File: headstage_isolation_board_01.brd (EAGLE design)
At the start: 100 x 80 mm, 15 parts

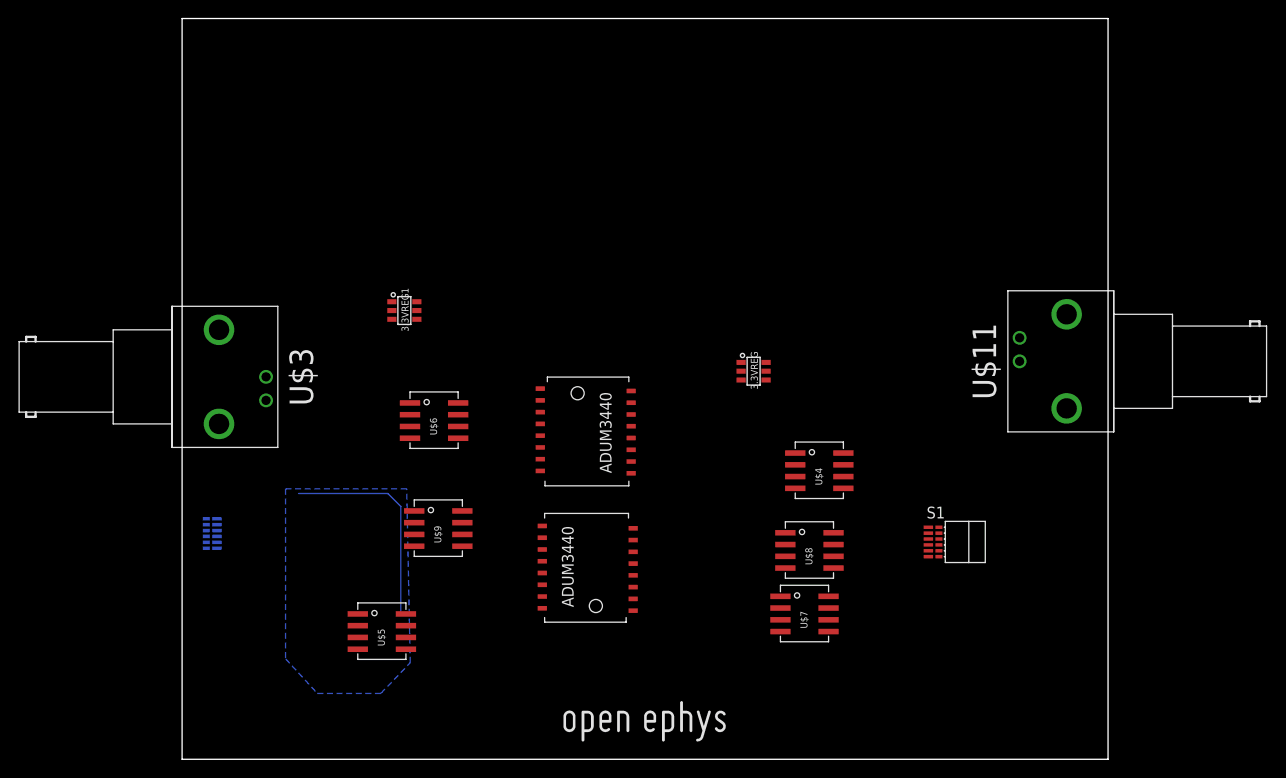
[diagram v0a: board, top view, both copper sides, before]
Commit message: added DC-DC converter
still missing resistors etc
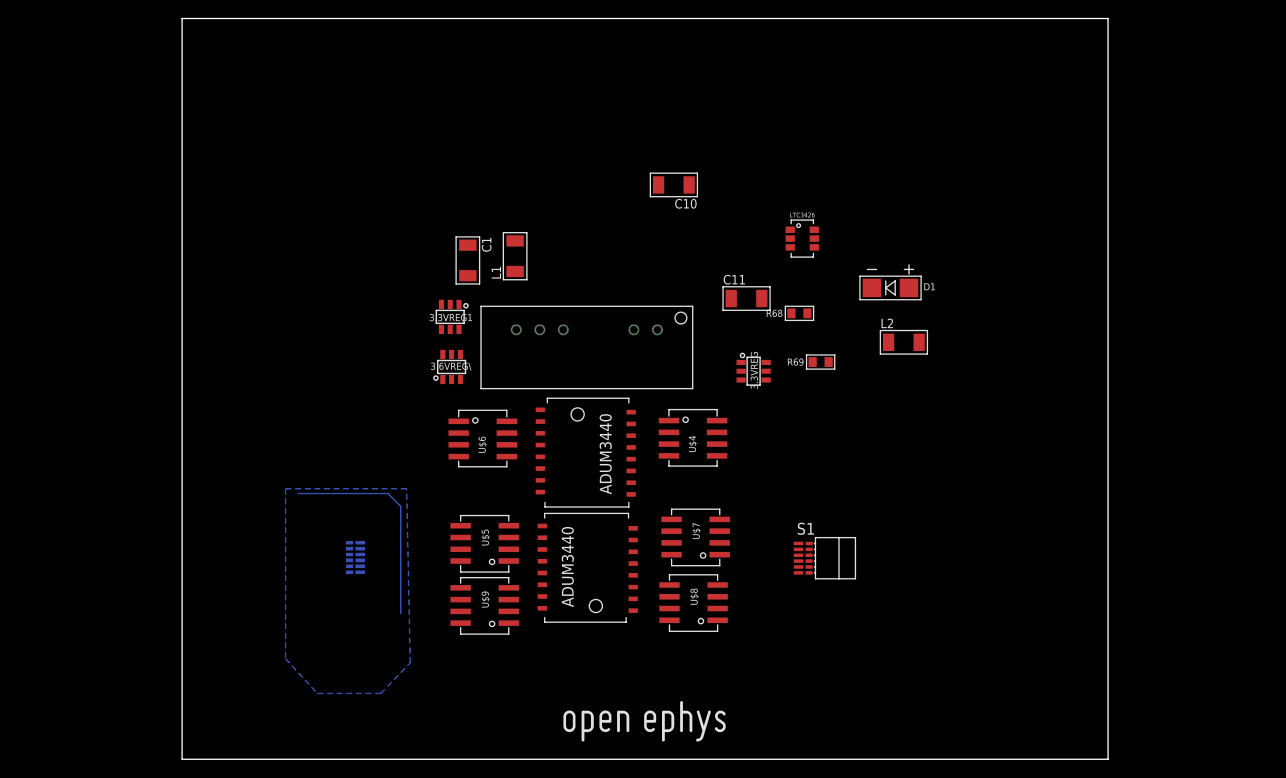
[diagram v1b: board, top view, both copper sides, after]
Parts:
- removed U$11, U$3: BNC_RIGHT_ANGLE, open-ephys_old:BNC_RIGHT_ANGLE
- added 3.6VREG\: TPS79301, RHD2000_eval_board:SOT-23-6
- added 5.5V_BOOST: LTC3426, open-ephys:SOT23-6
- added C1: 1u, RHD2000_eval_board:1206
- added C10, C11: 10u, RHD2000_eval_board:1206
- added D1: MBRA210LT3-D, open-ephys:MBRA210LT3-D
- added L1: 22uH, RHD2000_eval_board:1206
- added L2: (no value), RHD2000_eval_board:1206
- added R68: 95.3k, RHD2000_eval_board:0603
- added R69: 27.4k, RHD2000_eval_board:0603
- added U$12: NMV0505, open-ephys:NMV0505
- moved U$5 21.1 mm to (35.3, 25.2), turned to 180 degrees
- moved S2 15.7 mm to (17.1, 21.8)
- moved S1 14.1 mm to (68.7, 21.7)
- moved U$4 14.1 mm to (52.6, 32.8)
- moved U$7 13.8 mm to (58.1, 25.9), turned to 180 degrees
- moved U$9 11.2 mm to (35.3, 18.5), turned to 180 degrees
- moved U$8 7.54 mm to (57.8, 18.8), turned to 180 degrees
- moved U$6 5.62 mm to (29.9, 32.7)
- moved 3.3VREG1 5.00 mm to (29.0, 47.8), turned to 270 degrees
- moved U$10 2.29 mm to (42.7, 33.7)
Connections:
- removed net IN: 3.3VREG1.1
- removed net N$31: 3.3VREG.1, S1.T6
- new net 5VBOOST: 3.3VREG.1, 5.5V_BOOST.5, C11.1, D1.NEG, R68.2, U$12.P$1
- new net N$276: 5.5V_BOOST.3, R68.1, R69.2
- new net N$278: 5.5V_BOOST.1, D1.POS, L2.2
- new net N$32: L1.1, U$12.P$7
- new net N$34: 3.3VREG1.1, 3.6VREG\.1, C1.1, L1.2
- new net VDD_IN: 5.5V_BOOST.4, 5.5V_BOOST.6, C10.1, L2.1, S1.T6
- net GND: now also 5.5V_BOOST.2, C10.2, C11.2, R69.1, U$12.P$2; no longer U$11.P$GND
- net GND_ISOLATED: now also 3.6VREG\.2, C1.2, U$10.P2, U$10.P8, U$12.P$5, U$2.P15, U$2.P9, U$5.P4, U$6.P5, U$9.P4; no longer U$3.P$GND
- net VDD33_ISOLATED: now also U$10.P1, U$2.P16, U$5.P1, U$6.P8, U$9.P1
- net VDD_ISOLATED: now also 3.6VREG\.6

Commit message: initial partial layout, added some regulator parts
still need to change r values for regulators
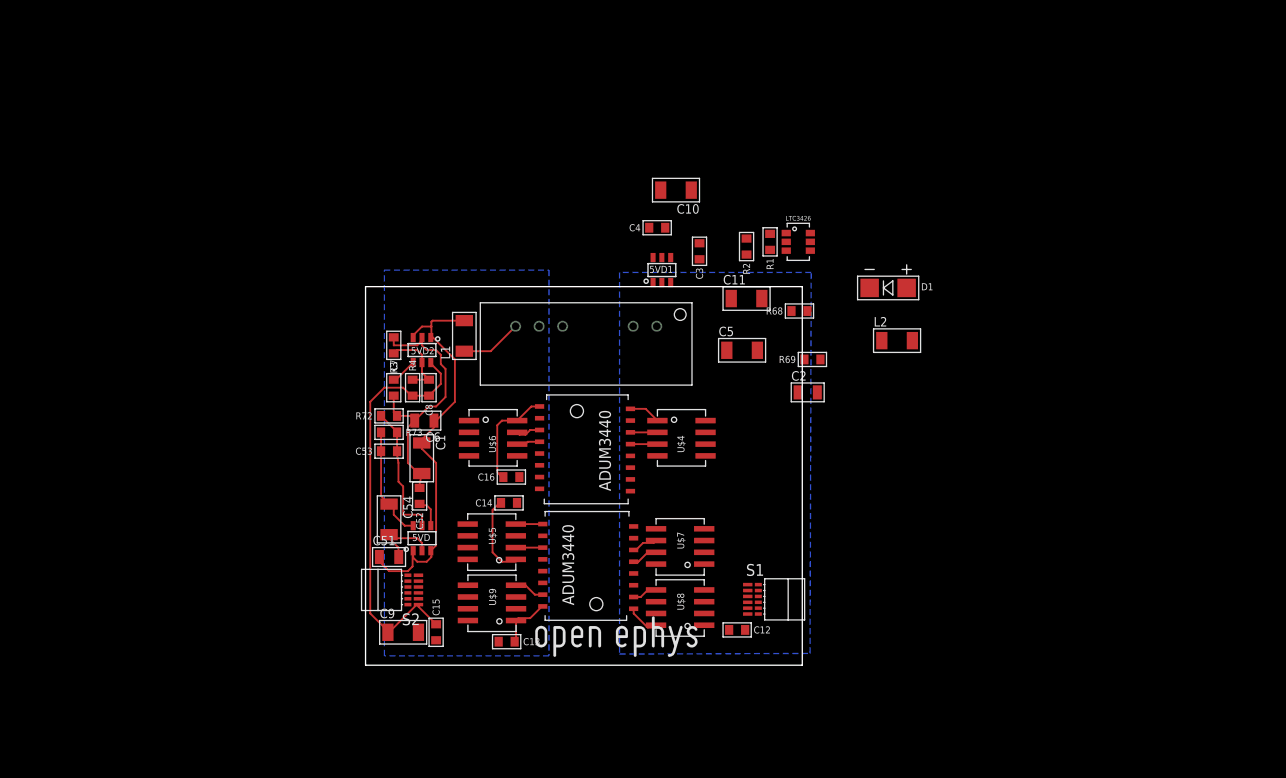
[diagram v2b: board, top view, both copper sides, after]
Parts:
- removed 3.3VREG, 3.3VREG1, 3.6VREG\: TPS79301, RHD2000_eval_board:SOT-23-6
- added 5VD, 5VD1, 5VD2: TPS79301, RHD2000_eval_board:SOT-23-6
- added C12, C13, C14, C15, C16: 100n, RHD2000_eval_board:0603
- added C2, C51, C6: 1.0u, RHD2000_eval_board:0805
- added C3, C52, C7: 10n, RHD2000_eval_board:0603
- added C4, C53, C8: 15p, RHD2000_eval_board:0603
- added C5, C54, C9: 22u, RHD2000_eval_board:1206
- added R1, R3, R72: 30.9k, RHD2000_eval_board:0603
- added R2, R4, R73: 95.3k, RHD2000_eval_board:0603
- moved C1 21.9 mm to (25.9, 32.5)
- moved L1 10.2 mm to (30.5, 45.7)
- moved U$1 9.64 mm to (37.5, 10.6)
- moved S2 7.21 mm to (23.4, 18.3), flipped to the top, turned to 90 degrees
- moved S1 7.06 mm to (63.2, 17.3)
- moved U$7 1.96 mm to (56.4, 24.9)
- moved U$8 1.54 mm to (56.4, 18.3)
- moved U$4 1.24 mm to (51.3, 32.8)
- moved U$6 1.12 mm to (31.0, 32.8)
- moved R69 0.93 mm to (68.1, 43.2)
- moved U$9 0.84 mm to (36.1, 18.8)
- moved U$5 0.78 mm to (36.0, 25.4)
- moved L2 0.76 mm to (77.2, 45.2)
- moved C10 0.60 mm to (53.3, 61.5)
- moved 5.5V_BOOST 0.56 mm to (66.5, 55.9)
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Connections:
- removed net N$34: 3.3VREG1.1, 3.6VREG\.1, C1.1, L1.2
- new net 5V_ISOLATED: 5VD.1, 5VD.3, 5VD2.1, 5VD2.3, C1.1, C51.1, C6.1, L1.2
- new net GND4: C15.2
- new net N$108: 5VD.5, C53.2, R72.1, R73.1
- new net N$33: 5VD1.4, C3.1
- new net N$35: 5VD1.5, C4.2, R1.1, R2.1
- new net N$36: 5VD2.4, C7.1
- new net N$37: 5VD2.5, C8.2, R3.1, R4.1
- new net N$97: 5VD.4, C52.1
- net 5VBOOST: now also 5VD1.1, 5VD1.3, C2.1; no longer 3.3VREG.1
- net GND: now also 5VD1.2, C12.1, C2.2, C3.2, C5.2, R1.2; no longer 3.3VREG.2
- net GND_ISOLATED: now also 5VD.2, 5VD2.2, C13.2, C14.2, C16.2, C51.2, C52.2, C54.2, C6.2, C7.2, C9.2, R3.2, R72.2, U$12.P$6; no longer 3.3VREG1.2, 3.6VREG\.2
- net VDD33: now also 5VD1.6, C12.2, C4.1, C5.1, R2.2; no longer 3.3VREG.6
- net VDD33_ISOLATED: now also 5VD.6, C13.1, C14.1, C16.1, C53.1, C54.1, R73.2; no longer 3.3VREG1.6
- net VDD_ISOLATED: now also 5VD2.6, C15.1, C8.1, C9.1, R4.2; no longer 3.6VREG\.6
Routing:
- net VDD_ISOLATED: track 0.00 -> 45.0 mm
- net 5V_ISOLATED: track 0.00 -> 44.8 mm
- net GND_ISOLATED: track 0.00 -> 44.2 mm
- net VDD33_ISOLATED: track 0.00 -> 37.8 mm
- net GND: track 23.2 -> 2.74 mm
- net N$108: track 0.00 -> 14.8 mm
- net N$37: track 0.00 -> 8.19 mm
- net VDD33: track 0.00 -> 7.10 mm
- net N$32: track 0.00 -> 6.65 mm
- net N$97: track 0.00 -> 3.21 mm
- net N$6: track 0.00 -> 2.91 mm
- net N$5: track 0.00 -> 2.91 mm
- net N$28: track 0.00 -> 2.91 mm
- net N$36: track 0.00 -> 2.86 mm
- net N$26: track 0.00 -> 2.84 mm
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- added copper zone on layer 16, net GND_ISOLATED
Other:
- board size 100 x 80 mm -> 47.2 x 40.9 mm

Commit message: more layout of power side
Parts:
- moved C10 31.6 mm to (63.5, 31.5), turned to 270 degrees
- moved 5.5V_BOOST 19.7 mm to (62.5, 36.6), turned to 180 degrees
- moved L2 19.4 mm to (66.5, 29.0), turned to 90 degrees
- moved D1 18.2 mm to (66.4, 35.6), turned to 90 degrees
- moved C4 15.4 mm to (64.0, 48.8)
- moved R1 13.4 mm to (65.5, 42.7), turned to 180 degrees
- moved 5VD1 12.4 mm to (62.0, 45.7), turned to 0 degrees
- moved R2 11.1 mm to (65.5, 45.2)
- moved R68 9.20 mm to (60.3, 41.8), turned to 90 degrees
- moved C16 8.64 mm to (35.6, 39.1), turned to 180 degrees
- moved C12 8.38 mm to (51.8, 11.9)
- moved C3 7.62 mm to (60.5, 48.8), turned to 180 degrees
- moved R69 5.79 mm to (62.5, 41.7), turned to 270 degrees
- moved C11 5.04 mm to (56.9, 46.7), turned to 90 degrees
- moved C5 4.72 mm to (57.4, 40.6), turned to 270 degrees
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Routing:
- net 5VBOOST: track 0.00 -> 33.8 mm
- net GND: track 2.74 -> 34.1 mm
- net VDD33: track 7.10 -> 38.0 mm, vias 0 -> 2
- net N$278: track 0.00 -> 12.4 mm
- net N$35: track 0.00 -> 8.21 mm
- net VDD33_ISOLATED: track 37.8 -> 29.7 mm
- net N$276: track 0.00 -> 7.88 mm, vias 0 -> 2
- net VDD_IN: track 0.00 -> 7.54 mm
- net N$33: track 0.00 -> 5.42 mm
- net GND_ISOLATED: track 44.2 -> 46.7 mm
- added copper zone on layer 1, net GND
- added copper zone on layer 1, net GND_ISOLATED
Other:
- board size 47.2 x 40.9 mm -> 48.7 x 40.9 mm

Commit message: initial rough layout
still missing correct resistor values
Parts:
- moved C9 13.9 mm to (21.8, 27.4), turned to 270 degrees
- moved C12 13.3 mm to (65.0, 13.5)
- moved C52 13.2 mm to (27.9, 41.4), turned to 180 degrees
- moved C54 13.0 mm to (26.9, 38.1), turned to 0 degrees
- moved C1 10.00 mm to (23.4, 42.2), turned to 180 degrees
- moved 5VD 8.52 mm to (23.4, 32.0), turned to 180 degrees
- moved C8 7.69 mm to (27.7, 47.8)
- moved C6 7.47 mm to (27.4, 43.9), turned to 270 degrees
- moved C51 6.43 mm to (24.4, 27.9), turned to 270 degrees
- moved C7 5.18 mm to (21.8, 45.2)
- moved U$1 4.64 mm to (32.9, 9.83)
- moved R4 4.60 mm to (24.4, 44.7), turned to 0 degrees
- moved R3 3.94 mm to (21.8, 48.5)
- moved 5VD2 3.87 mm to (24.4, 47.8)
- moved C13 3.59 mm to (31.5, 12.2)
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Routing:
- net VDD33: track 38.0 -> 77.1 mm
- net VDD33_ISOLATED: track 29.7 -> 63.8 mm, vias 0 -> 2
- net N$13: track 0.00 -> 27.1 mm
- net N$10: track 0.00 -> 26.8 mm
- net N$2: track 0.00 -> 23.9 mm
- net N$11: track 0.00 -> 23.3 mm
- net N$12: track 0.00 -> 22.8 mm
- net N$3: track 0.00 -> 22.4 mm
- net N$1: track 0.00 -> 21.5 mm
- net N$4: track 0.00 -> 20.5 mm, vias 0 -> 2
- net VDD_IN: track 7.54 -> 24.6 mm, vias 0 -> 2
- net N$20: track 0.00 -> 14.5 mm, vias 0 -> 2
- net N$16: track 0.00 -> 14.2 mm, vias 0 -> 2
- net N$17: track 0.00 -> 13.8 mm
- net N$21: track 0.00 -> 13.5 mm
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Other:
- board size 48.7 x 40.9 mm -> 50 x 40.9 mm
- board text added: "RHD decoupling"
- board text added: "aq. board"
- board text added: "headstage"
- board text added: "module"
- board text added: "rev 1.0"

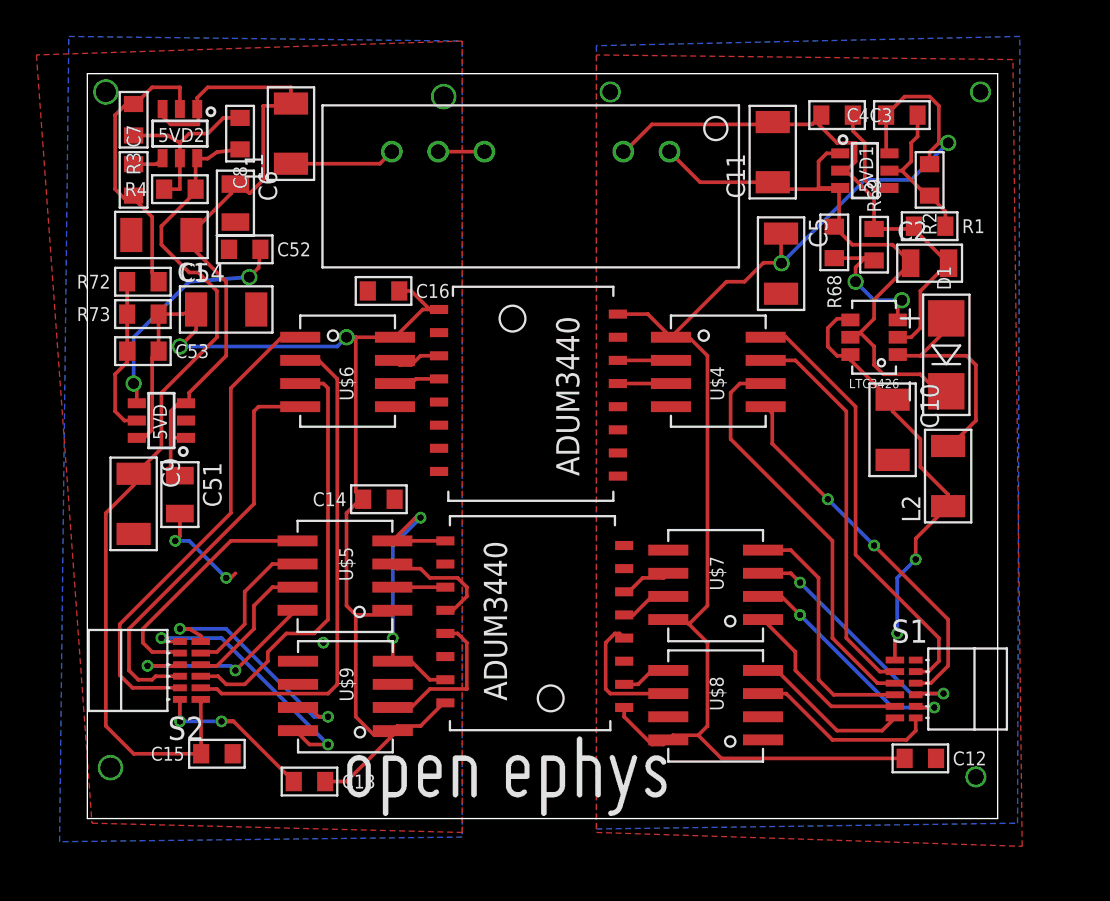
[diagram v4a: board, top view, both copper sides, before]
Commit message: routing cleanup, added more bypass caps
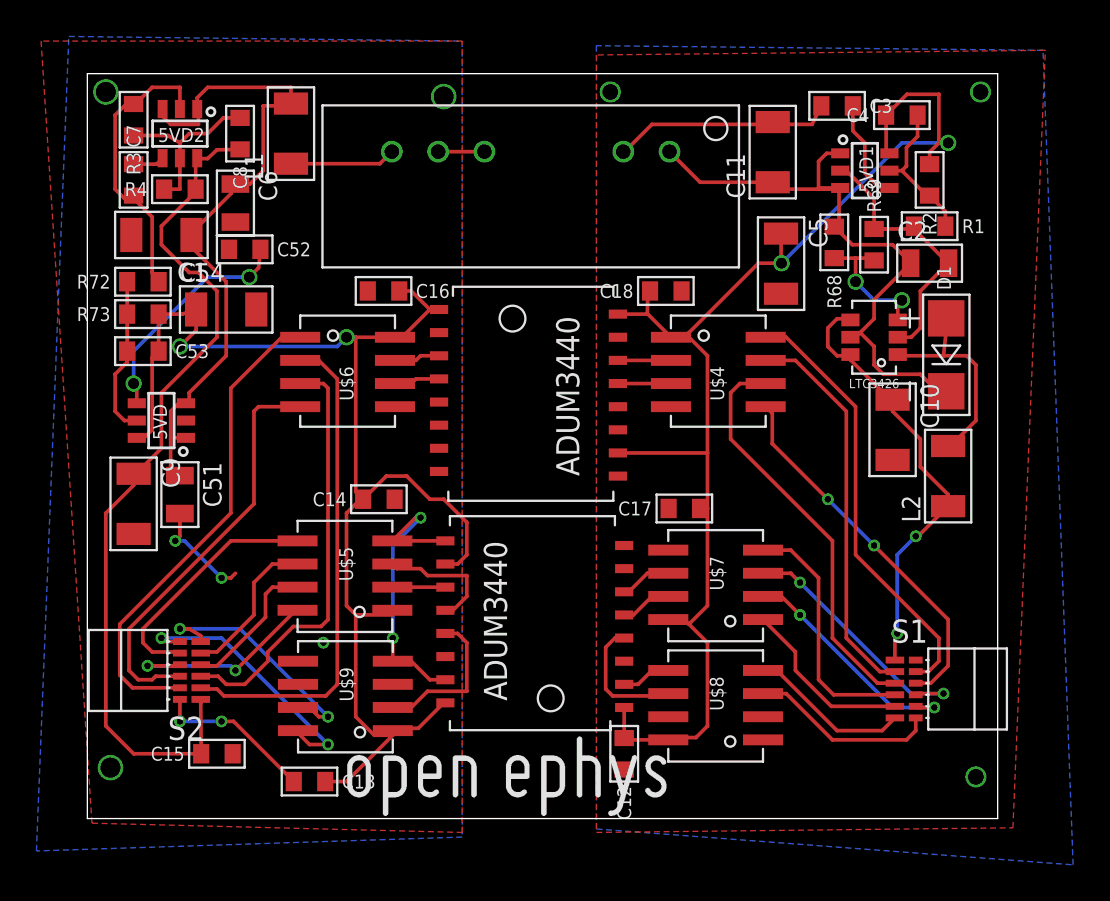
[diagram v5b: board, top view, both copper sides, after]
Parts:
- added C17, C18: 100n, RHD2000_eval_board:0603
- moved C12 16.3 mm to (48.8, 13.7), turned to 90 degrees
- moved C3 0.51 mm to (60.5, 49.3)
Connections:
- net GND: now also C17.1, C18.2
- net VDD33: now also C17.2, C18.1, U$10.P10
- net VDD33_ISOLATED: now also U$2.P10
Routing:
- net VDD33_ISOLATED: track 63.8 -> 74.2 mm
- net VDD33: track 77.1 -> 72.1 mm
- net GND: track 34.1 -> 30.3 mm
- net GND_ISOLATED: track 50.9 -> 50.3 mm
- net 5V_ISOLATED: track 37.6 -> 37.0 mm
- net N$278: track 12.4 -> 11.8 mm
